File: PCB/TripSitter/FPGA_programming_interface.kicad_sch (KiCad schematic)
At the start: 10 parts, among them IC1 MT25QL256ABA1EW9-0SIT, J1 Conn_ARM_JTAG_SWD_20, U1 XC7A100T-FGG484

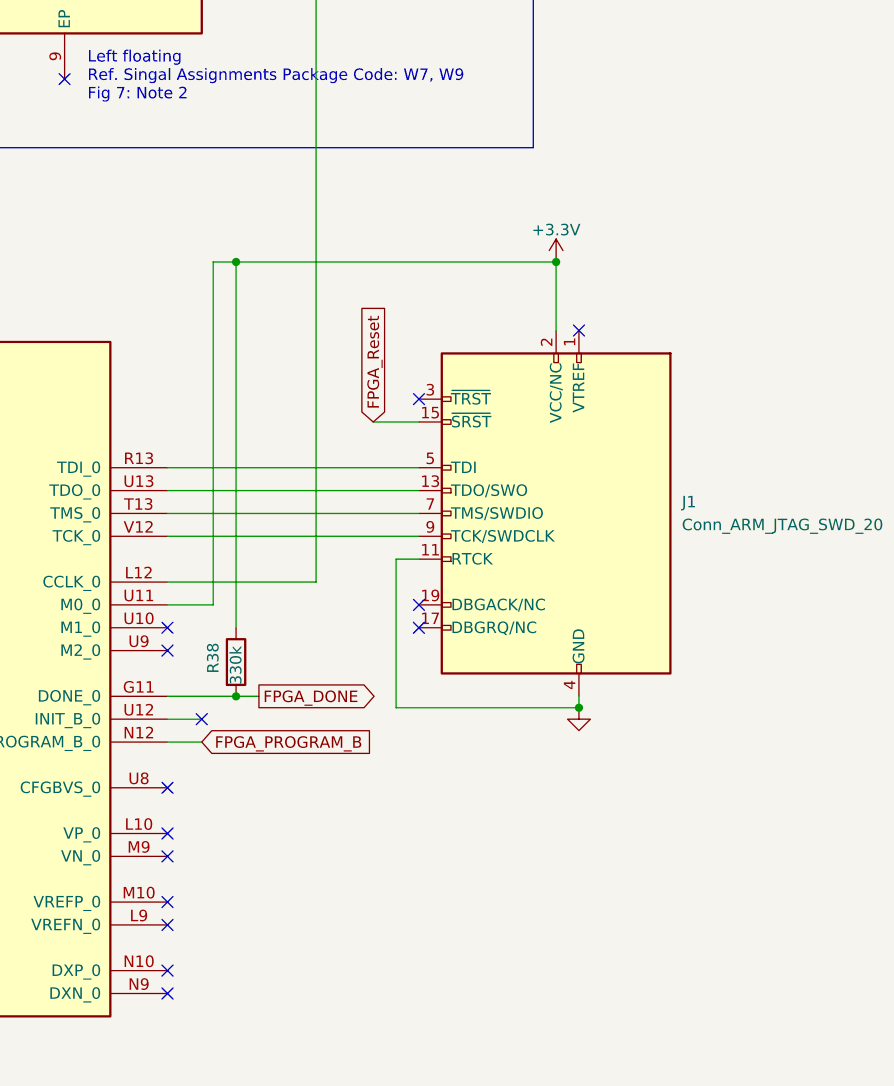
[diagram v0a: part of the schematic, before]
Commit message: pcb: re-structured PCB schematic layout (#17)
Co-authored-by: Sigvart Hovland <sigvart.m@gmail.com>
Co-authored-by: Ida-Sofie Pettersen <idasofie@Ida-Sofies-MacBook-Air.local>
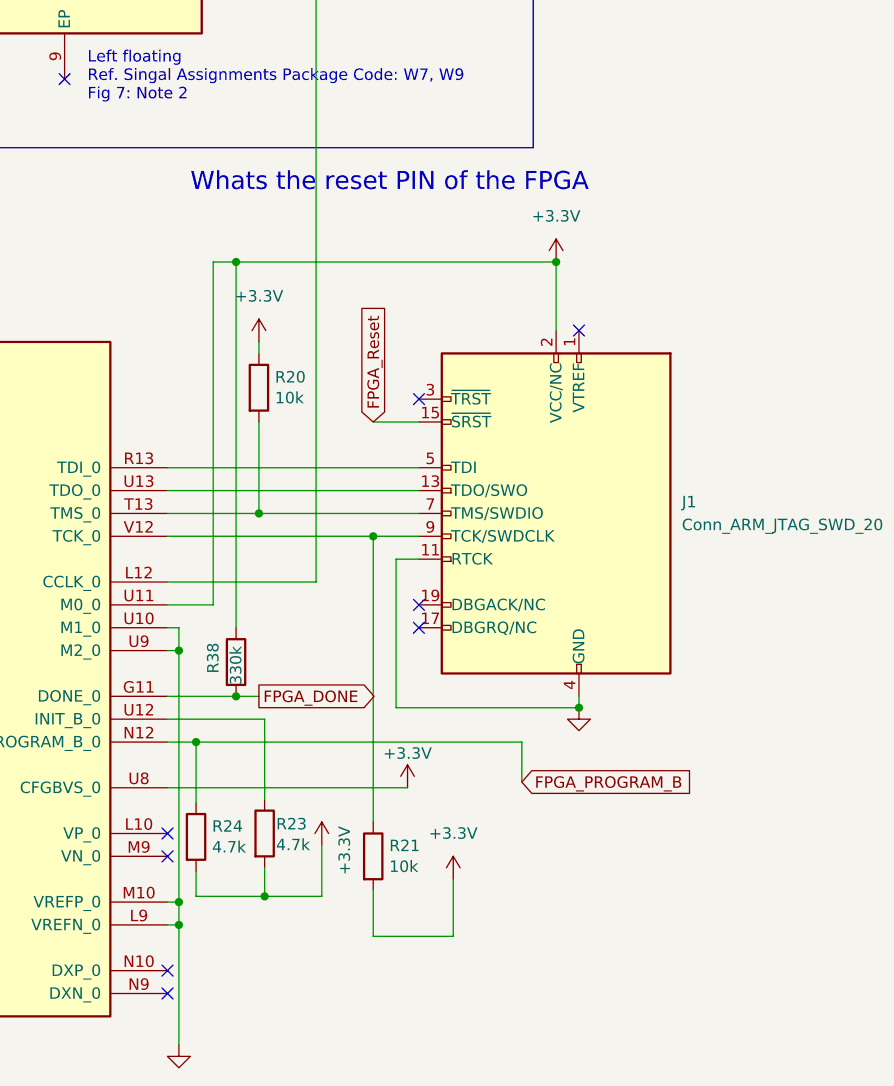
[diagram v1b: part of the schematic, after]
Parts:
- added R20, R21: 10k, Resistor_SMD:R_0805_2012Metric_Pad1.20x1.40mm_HandSolder, symbol Device:R
- added R23, R24: 4.7k, Resistor_SMD:R_0603_1608Metric_Pad0.98x0.95mm_HandSolder, symbol Device:R
- C39: footprint Capacitor_SMD:C_1210_3225Metric_Pad1.33x2.70mm_HandSolder -> Capacitor_SMD:C_0603_1608Metric_Pad1.08x0.95mm_HandSolder; Component name CL21A476MQYNNNG -> CL10A476MR8NZNE; DK_Detail_Page https://www.digikey.no/product-detail/no/murata-electronics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 -> https://www.digikey.no/no/products/detail/samsung-electro-m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
- J1: footprint Connector_PinHeader_1.00mm:PinHeader_2x10_P1.00mm_Vertical -> Connector_PinHeader_2.54mm:PinHeader_2x07_P2.54mm_Vertical_SMD
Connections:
- net +3V3 is gone; now on net +3.3V: J1.2 (VCC/NC), R38.1, U1.U11 (M0_0)
- net +3.3V: now also U1.U8 (CFGBVS_0), R20.1, R21.2, R23.2, R24.2
- net FPGA_PROGRAM_B: now also R24.1
- net GND: now also U1.L9 (VREFN_0), U1.M10 (VREFP_0), U1.U10 (M1_0), U1.U9 (M2_0)
- net at J1.7 (TMS/SWDIO), U1.T13 (TMS_0): now also R20.2
- net at U1.U12 (INIT_B_0): now also R23.1
- net at J1.9 (TCK/SWDCLK), U1.V12 (TCK_0): now also R21.1
- no-connect marks 15 -> 9
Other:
- note added: "Whats the reset PIN of the FPGA"
